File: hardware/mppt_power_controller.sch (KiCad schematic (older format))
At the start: 32 parts

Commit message: Add LT3080 as 3.3V regulator, remove input/output solar and battery protection, add ARM JTAG connector, all symbols now have footprints.
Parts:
- removed D? (x2): D_TVS_ALT, symbol Device:D_TVS_ALT
- removed F? (x2): Polyfuse, symbol Device:Polyfuse
- removed Q? (x2): Q_NMOS_GDS, symbol Device:Q_NMOS_GDS
- added C10: 10uF, Capacitor_SMD:C_0805_2012Metric_Pad1.15x1.40mm_HandSolder, symbol Device:C_Small
- added J2: Conn_ARM_JTAG_SWD_10, Connector_PinHeader_1.27mm:PinHeader_2x05_P1.27mm_Vertical_SMD, symbol Connector:Conn_ARM_JTAG_SWD_10
- added Q1, Q2: Q_NMOS_GSD, Package_TO_SOT_SMD:SOT-23, symbol Device:Q_NMOS_GSD
- added R10: 330k, Resistor_SMD:R_0603_1608Metric_Pad1.05x0.95mm_HandSolder, symbol Device:R_Small
- added U5: LT3080xST, Package_TO_SOT_SMD:SOT-223, symbol Regulator_Linear:LT3080xST
- C1, C7: renamed from C?; footprint (none) -> Capacitor_SMD:C_0603_1608Metric_Pad1.05x0.95mm_HandSolder
- R3, R4: renamed from R?; value 1.5k -> 4.7k
- gave numbers to parts that had none: 22
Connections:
- wire segments 142 -> 140
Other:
- note added: "Battery Voltage/Current Monitor"
- note added: "Solar Panel Current/Voltage Monitor"
- note added: "~~20mA max on 3.3V rail for the micro, INA233s, and status LEDs.\n??mA for FET gate driver and curiosity board/LCD"
- moved on the sheet: C1, C5, C6, C7, C8, C9, J3, L2, R5, R6, R7, R8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

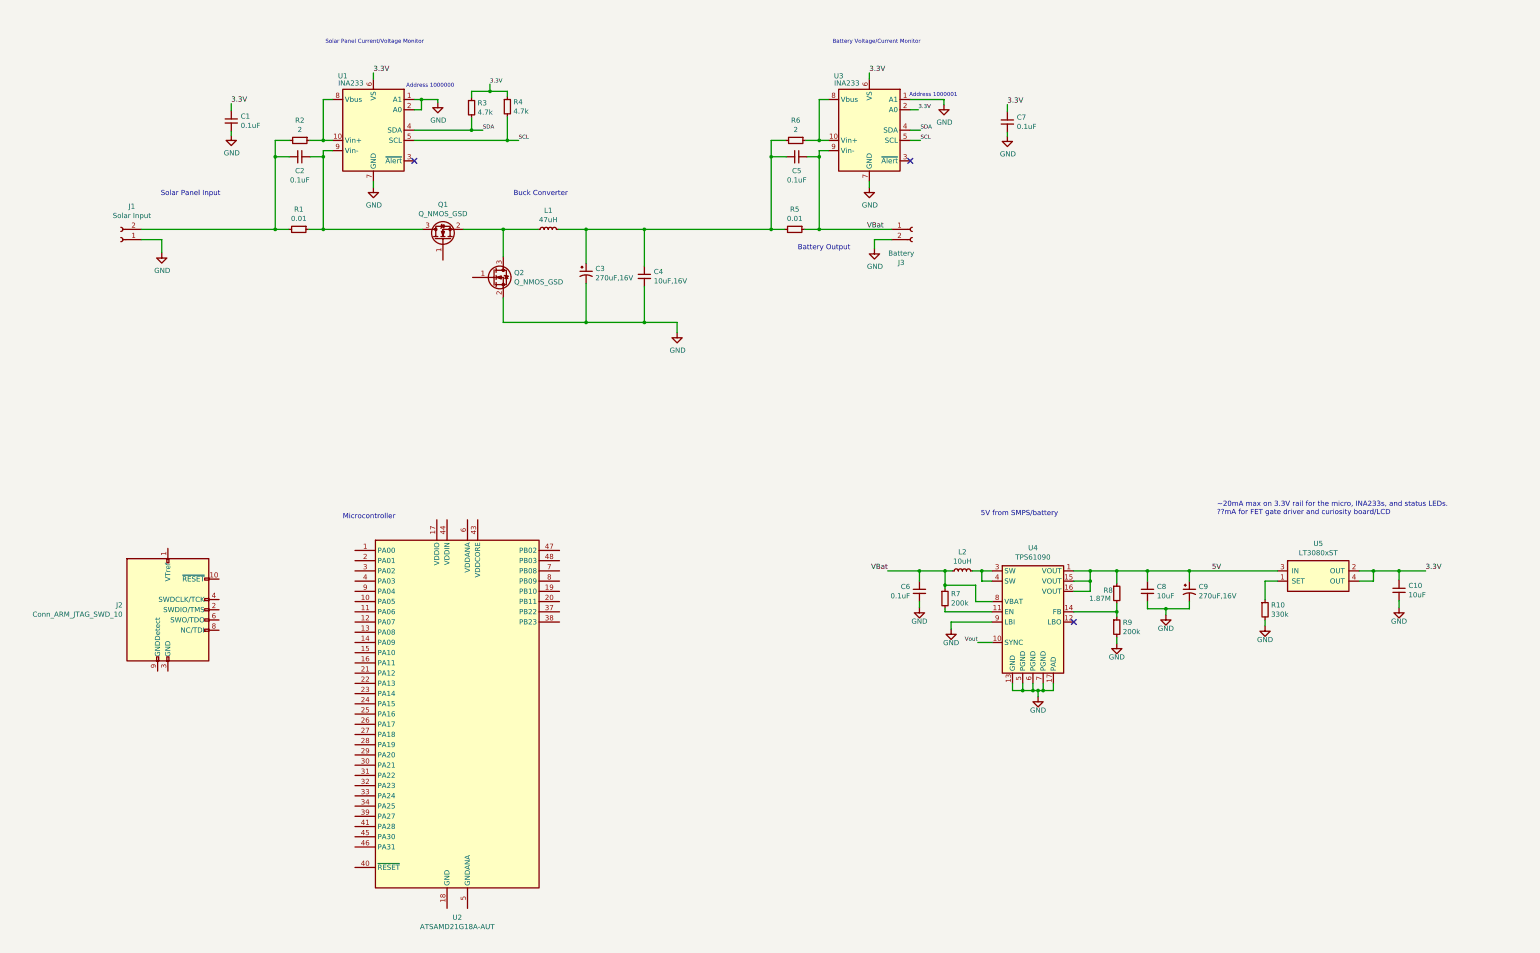
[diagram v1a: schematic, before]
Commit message: Wire up most of microcontroller, add some placeholder outputs, fix a small mistake on the TPS61090 boost controller.
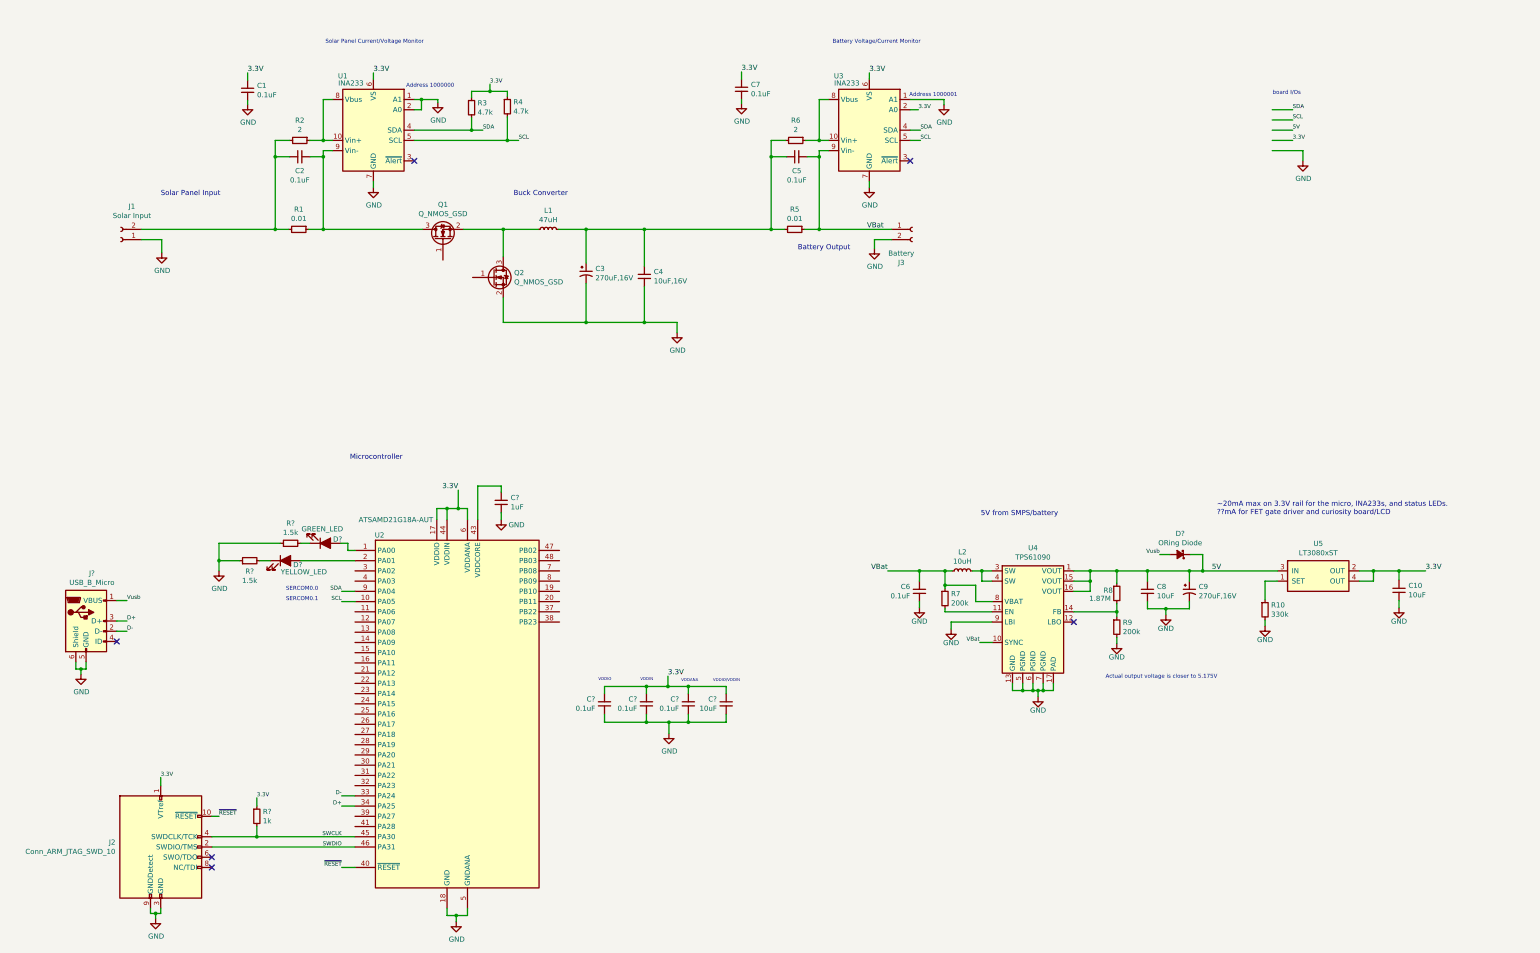
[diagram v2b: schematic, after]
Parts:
- added C? (x3): 0.1uF, Capacitor_SMD:C_0603_1608Metric_Pad1.05x0.95mm_HandSolder, symbol Device:C_Small
- added C?: 1uF, Capacitor_SMD:C_0603_1608Metric_Pad1.05x0.95mm_HandSolder, symbol Device:C_Small
- added C?: 10uF, Capacitor_SMD:C_0805_2012Metric_Pad1.15x1.40mm_HandSolder, symbol Device:C_Small
- added D?: ORing Diode, Diode_SMD:D_SMB_Handsoldering, symbol Device:D_Schottky_Small_ALT
- added D?: GREEN_LED, symbol Device:LED_ALT
- added D?: YELLOW_LED, symbol Device:LED_ALT
- added J?: USB_B_Micro, symbol Connector:USB_B_Micro
- added R?: 1k, Resistor_SMD:R_0603_1608Metric_Pad1.05x0.95mm_HandSolder, symbol Device:R_Small
- added R? (x2): 1.5k, Resistor_SMD:R_0603_1608Metric_Pad1.05x0.95mm_HandSolder, symbol Device:R_Small
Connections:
- net Vout is gone; now on net VBat: U4.10 (SYNC)
- net 3.3V: now also J2.1 (VTref), U2.17 (VDDIO), U2.36 (VDDIO), U2.44 (VDDIN), U2.6 (VDDANA), C?.1, C?.2, C?.2, C?.2, R?.1
- net 5V: now also D?.1 (K)
- net GND: now also J2.3 (GND), J2.5 (GND), J2.9 (GNDDetect), U2.18 (GND), U2.35 (GND), U2.42 (GND), U2.5 (GNDANA), C?.1, C?.1, C?.1, C?.1, C?.2, J?.5 (GND), J?.6 (Shield), R?.1, R?.1
- net SCL: now also U2.10 (PA05)
- net SDA: now also U2.9 (PA04)
- net ~RESET: now reaches J2.10 (~RESET~)
- net ~RESET: now also U2.40 (~RESET)
- net SWDIO: now reaches J2.2 (SWDIO/TMS)
- net SWDIO: now also U2.46 (PA31)
- net SWCLK: now reaches J2.4 (SWDCLK/TCK)
- net SWCLK: now also U2.45 (PA30), R?.2
- net at U2.1 (PA00): now also D?.2 (A)
- net at U2.2 (PA01): now also D?.2 (A)
- net D-: now reaches U2.33 (PA24)
- net D-: now also J?.2 (D-)
- net D+: now reaches U2.34 (PA25)
- net D+: now also J?.3 (D+)
- net at U2.43 (VDDCORE): now also C?.2
- new net: D?.1 (K), R?.2 (x2)
- new net Vusb: D?.2 (A), J?.1 (VBUS)
- no-connect marks 3 -> 6
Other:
- note added: "Actual output voltage is closer to 5.175V"
- note added: "SERCOM0.0"
- note added: "SERCOM0.1"
- note added: "VDDANA"
- note added: "VDDIN"
- note added: "VDDIO"
- note added: "VDDIO/VDDIN"
- note added: "board I/Os"
- moved on the sheet: C1, C7, J2

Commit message: Add PX3519 synchronous FET driver, a handful of testpoints, and clear ERC.
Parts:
- added C3: 0.1uF, Capacitor_SMD:C_0603_1608Metric_Pad1.05x0.95mm_HandSolder, symbol Device:C_Small
- added C4: 1nF, symbol Device:C_Small
- added J5: Curiosity Board, Connector_PinSocket_2.54mm:PinSocket_1x05_P2.54mm_Vertical, symbol Connector:Conn_01x05_Male
- added TP1: Solar, TestPoint:TestPoint_Keystone_5019_Minature, symbol Connector:TestPoint
- added TP2: PWM, TestPoint:TestPoint_Keystone_5019_Minature, symbol Connector:TestPoint
- added TP3: SDA, TestPoint:TestPoint_Keystone_5019_Minature, symbol Connector:TestPoint
- added TP4: SCL, TestPoint:TestPoint_Keystone_5019_Minature, symbol Connector:TestPoint
- added TP5: 5V, TestPoint:TestPoint_Keystone_5019_Minature, symbol Connector:TestPoint
- added TP6: 3.3V, TestPoint:TestPoint_Keystone_5019_Minature, symbol Connector:TestPoint
- added TP7: GND, TestPoint:TestPoint_Keystone_5019_Minature, symbol Connector:TestPoint
- added U2: PX3519, Package_SON:WSON-8-1EP_3x3mm_P0.5mm_EP1.6x2.0mm, symbol Driver_FET:PX3519
- D1, D2: renamed from D?; footprint (none) -> LED_SMD:LED_0603_1608Metric_Pad1.05x0.95mm_HandSolder
- J2: renamed from J?; footprint (none) -> Connector_USB:USB_Micro-B_Amphenol_10103594-0001LF_Horizontal
- U1: symbol Analog_ADC:INA233 -> mppt_power_controller-rescue:INA233-Analog_ADC
- U4: renamed from U3; symbol Analog_ADC:INA233 -> mppt_power_controller-rescue:INA233-Analog_ADC
- gave numbers to parts that had none: 9
- renumbered C7 to C12, C5 to C13, C6 to C14, C8 to C15, C9 to C16, C10 to C17, C3 to C6, C4 to C8, J2 to J3, J3 to J4, R7 to R10, R8 to R11, R9 to R12, R10 to R13, R3 to R6, R4 to R7, R5 to R8, R6 to R9, U2 to U3, U4 to U5, U5 to U6
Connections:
- net 3.3V: now also J5.4 (Pin_4), TP6.1
- net 5V: now also C3.1, J5.3 (Pin_3), TP5.1, U2.4 (VCC)
- net GND: now also C3.2, J5.5 (Pin_5), TP7.1, U2.6 (GND), U2.9 (EP)
- net SCL: now also J5.2 (Pin_2), TP4.1
- net SDA: now also J5.1 (Pin_1), TP3.1
- net at C2.2, J1.2 (Pin_2), R1.2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: now also TP1.1
- net at L1.1, Q1.2 (S), Q2.3 (D): now also C4.1, U2.7 (PHASE)
- net at Q1.1 (G): now also U2.8 (UGATE)
- net at Q2.1 (G): now also U2.5 (LGATE)
- net FET_PWM: now reaches U3.15 (PA10)
- net FET_PWM: now also TP2.1, U2.2 (PWM)
- net FET_ENABLE: now reaches U3.16 (PA11)
- net FET_ENABLE: now also U2.3 (EN)
- new net: C4.2, U2.1 (BOOT)
- no-connect marks 6 -> 34
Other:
- note added: "5V@900mA from SMPS/battery"
- note removed: "5V from SMPS/battery"
- moved on the sheet: C1, C2, J1, Q1, R1, R2, R6, R7, U1
